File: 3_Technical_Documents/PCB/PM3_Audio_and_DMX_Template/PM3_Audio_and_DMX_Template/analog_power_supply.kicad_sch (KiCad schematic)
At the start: 16 parts, among them U6 TLV61070ADBV, U7 LT3045xMSE

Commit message: new push
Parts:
- renumbered C18 to C19, C19 to C20, C20 to C21, C21 to C22, C22 to C23, C23 to C24, C24 to C25, R25 to R21, R26 to R22, R27 to R23, R28 to R24, R29 to R25, R30 to R26, U6 to U7, U7 to U8
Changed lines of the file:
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@@
 		(dnp no)
 		(fields_autoplaced yes)
-		(property "Reference" "#PWR050"
+		(property "Reference" "#PWR058"
 			(at 92.71 106.68 0)
 			(effects
@@
 			(project ""
 				(path "/1f276d59-ad9b-4e70-a842-f3b7e562eb9b/2329d9ea-d5d7-4913-84c5-e85a54af032e/99ea690b-15c6-4a9d-8469-e6d453aade26"
-					(reference "#PWR050")
+					(reference "#PWR058")
 					(unit 1)
 				)
@@
 		(dnp no)
 		(fields_autoplaced yes)
-		(property "Reference" "R25"
+		(property "Reference" "R21"
 			(at 95.25 81.2799 0)
 			(effects
@@
 			(project ""
 				(path "/1f276d59-ad9b-4e70-a842-f3b7e562eb9b/2329d9ea-d5d7-4913-84c5-e85a54af032e/99ea690b-15c6-4a9d-8469-e6d453aade26"
-					(reference "R25")
+					(reference "R21")
 					(unit 1)
 				)
@@
 		(dnp no)
 		(fields_autoplaced yes)
-		(property "Reference" "U6"
+		(property "Reference" "U7"
 			(at 74.93 66.04 0)
 			(effects
@@
 			(project ""
 				(path "/1f276d59-ad9b-4e70-a842-f3b7e562eb9b/2329d9ea-d5d7-4913-84c5-e85a54af032e/99ea690b-15c6-4a9d-8469-e6d453aade26"
-					(reference "U6")
+					(reference "U7")
 					(unit 1)
 				)
@@
 		(dnp no)
 		(fields_autoplaced yes)
-		(property "Reference" "C18"
+		(property "Reference" "C19"
 			(at 40.64 77.8509 0)
 			(effects
@@
 			(project ""
 				(path "/1f276d59-ad9b-4e70-a842-f3b7e562eb9b/2329d9ea-d5d7-4913-84c5-e85a54af032e/99ea690b-15c6-4a9d-8469-e6d453aade26"
-					(reference "C18")
+					(reference "C19")
 					(unit 1)
 				)
@@
 		(dnp no)
 		(fields_autoplaced yes)
-		(property "Reference" "#PWR049"
+		(property "Reference" "#PWR057"
 			(at 74.93 97.79 0)
 			(effects
@@
 			(project ""
 				(path "/1f276d59-ad9b-4e70-a842-f3b7e562eb9b/2329d9ea-d5d7-4913-84c5-e85a54af032e/99ea690b-15c6-4a9d-8469-e6d453aade26"
-					(reference "#PWR049")
+					(reference "#PWR057")
 					(unit 1)
 				)
@@
 		(dnp no)
 		(fields_autoplaced yes)
-		(property "Reference" "#PWR057"
+		(property "Reference" "#PWR065"
 			(at 212.09 90.17 0)
 			(effects
@@
 			(project ""
 				(path "/1f276d59-ad9b-4e70-a842-f3b7e562eb9b/2329d9ea-d5d7-4913-84c5-e85a54af032e/99ea690b-15c6-4a9d-8469-e6d453aade26"
-					(reference "#PWR057")
+					(reference "#PWR065")
 					(unit 1)
 				)
@@
 		(on_board yes)
 		(dnp no)
-		(property "Reference" "C23"
+		(property "Reference" "C24"
 			(at 167.132 60.706 90)
 			(effects
@@
 			(project "PM3_Audio_and_DMX"
 				(path "/1f276d59-ad9b-4e70-a842-f3b7e562eb9b/2329d9ea-d5d7-4913-84c5-e85a54af032e/99ea690b-15c6-4a9d-8469-e6d453aade26"
-					(reference "C23")
+					(reference "C24")
 					(unit 1)
 				)
@@
 		(dnp no)
 		(fields_autoplaced yes)
-		(property "Reference" "R28"
+		(property "Reference" "R24"
 			(at 200.66 58.4199 0)
 			(effects
@@
 			(project ""
 				(path "/1f276d59-ad9b-4e70-a842-f3b7e562eb9b/2329d9ea-d5d7-4913-84c5-e85a54af032e/99ea690b-15c6-4a9d-8469-e6d453aade26"
-					(reference "R28")
+					(reference "R24")
 					(unit 1)
 				)
@@
 		(dnp no)
 		(fields_autoplaced yes)
-		(property "Reference" "#PWR052"
+		(property "Reference" "#PWR060"
 			(at 156.21 74.93 0)
 			(effects
@@
 			(project "PM3_Audio_and_DMX"
 				(path "/1f276d59-ad9b-4e70-a842-f3b7e562eb9b/2329d9ea-d5d7-4913-84c5-e85a54af032e/99ea690b-15c6-4a9d-8469-e6d453aade26"
-					(reference "#PWR052")
+					(reference "#PWR060")
 					(unit 1)
 				)
@@
 		(dnp no)
 		(fields_autoplaced yes)
-		(property "Reference" "R30"
+		(property "Reference" "R26"
 			(at 205.74 87.6299 0)
 			(effects
@@
 			(project ""
 				(path "/1f276d59-ad9b-4e70-a842-f3b7e562eb9b/2329d9ea-d5d7-4913-84c5-e85a54af032e/99ea690b-15c6-4a9d-8469-e6d453aade26"
-					(reference "R30")
+					(reference "R26")
 					(unit 1)
 				)
@@
 		(dnp no)
 		(fields_autoplaced yes)
-		(property "Reference" "#PWR051"
+		(property "Reference" "#PWR059"
 			(at 118.11 97.79 0)
 			(effects
@@
 			(project ""
 				(path "/1f276d59-ad9b-4e70-a842-f3b7e562eb9b/2329d9ea-d5d7-4913-84c5-e85a54af032e/99ea690b-15c6-4a9d-8469-e6d453aade26"
-					(reference "#PWR051")
+					(reference "#PWR059")
 					(unit 1)
 				)
@@
 		(dnp no)
 		(fields_autoplaced yes)
-		(property "Reference" "#PWR055"
+		(property "Reference" "#PWR063"
 			(at 185.42 91.44 0)
 			(effects
@@
 			(project ""
 				(path "/1f276d59-ad9b-4e70-a842-f3b7e562eb9b/2329d9ea-d5d7-4913-84c5-e85a54af032e/99ea690b-15c6-4a9d-8469-e6d453aade26"
-					(reference "#PWR055")
+					(reference "#PWR063")
 					(unit 1)
 				)
@@
 		(dnp no)
 		(fields_autoplaced yes)
-		(property "Reference" "#PWR054"
+		(property "Reference" "#PWR062"
 			(at 162.56 73.66 0)
 			(effects
@@
 			(project ""
 				(path "/1f276d59-ad9b-4e70-a842-f3b7e562eb9b/2329d9ea-d5d7-4913-84c5-e85a54af032e/99ea690b-15c6-4a9d-8469-e6d453aade26"
-					(reference "#PWR054")
+					(reference "#PWR062")
 					(unit 1)
 				)
@@
 		(dnp no)
 		(fields_autoplaced yes)
-		(property "Reference" "R29"
+		(property "Reference" "R25"
 			(at 205.74 77.4699 0)
 			(effects
@@
 			(project ""
 				(path "/1f276d59-ad9b-4e70-a842-f3b7e562eb9b/2329d9ea-d5d7-4913-84c5-e85a54af032e/99ea690b-15c6-4a9d-8469-e6d453aade26"
-					(reference "R29")
+					(reference "R25")
 					(unit 1)
 				)
@@
 		(dnp no)
 		(fields_autoplaced yes)
-		(property "Reference" "#PWR048"
+		(property "Reference" "#PWR056"
 			(at 52.07 93.98 0)
 			(effects
@@
 			(project ""
 				(path "/1f276d59-ad9b-4e70-a842-f3b7e562eb9b/2329d9ea-d5d7-4913-84c5-e85a54af032e/99ea690b-15c6-4a9d-8469-e6d453aade26"
-					(reference "#PWR048")
+					(reference "#PWR056")
 					(unit 1)
 				)
@@
 		(dnp no)
 		(fields_autoplaced yes)
-		(property "Reference" "#PWR047"
+		(property "Reference" "#PWR055"
 			(at 36.83 95.25 0)
 			(effects
@@
 			(project ""
 				(path "/1f276d59-ad9b-4e70-a842-f3b7e562eb9b/2329d9ea-d5d7-4913-84c5-e85a54af032e/99ea690b-15c6-4a9d-8469-e6d453aade26"
-					(reference "#PWR047")
+					(reference "#PWR055")
 					(unit 1)
 				)
@@
 		(dnp no)
 		(fields_autoplaced yes)
-		(property "Reference" "C22"
+		(property "Reference" "C23"
 			(at 153.67 81.2799 0)
 			(effects
@@
 			(project ""
 				(path "/1f276d59-ad9b-4e70-a842-f3b7e562eb9b/2329d9ea-d5d7-4913-84c5-e85a54af032e/99ea690b-15c6-4a9d-8469-e6d453aade26"
-					(reference "C22")
+					(reference "C23")
 					(unit 1)
 				)
@@
 		(dnp no)
 		(fields_autoplaced yes)
-		(property "Reference" "C19"
+		(property "Reference" "C20"
 			(at 55.88 78.7399 0)
 			(effects
@@
 			(project ""
 				(path "/1f276d59-ad9b-4e70-a842-f3b7e562eb9b/2329d9ea-d5d7-4913-84c5-e85a54af032e/99ea690b-15c6-4a9d-8469-e6d453aade26"
-					(reference "C19")
+					(reference "C20")
 					(unit 1)
 				)
@@
 		(dnp no)
 		(fields_autoplaced yes)
-		(property "Reference" "#PWR056"
+		(property "Reference" "#PWR064"
 			(at 203.2 102.87 0)
 			(effects
@@
 			(project ""
 				(path "/1f276d59-ad9b-4e70-a842-f3b7e562eb9b/2329d9ea-d5d7-4913-84c5-e85a54af032e/99ea690b-15c6-4a9d-8469-e6d453aade26"
-					(reference "#PWR056")
+					(reference "#PWR064")
 					(unit 1)
 				)
@@
 		(dnp no)
 		(fields_autoplaced yes)
-		(property "Reference" "R26"
+		(property "Reference" "R22"
 			(at 95.25 91.4399 0)
 			(effects
@@
 			(project ""
 				(path "/1f276d59-ad9b-4e70-a842-f3b7e562eb9b/2329d9ea-d5d7-4913-84c5-e85a54af032e/99ea690b-15c6-4a9d-8469-e6d453aade26"
-					(reference "R26")
+					(reference "R22")
 					(unit 1)
 				)
@@
 		(dnp no)
 		(fields_autoplaced yes)
-		(property "Reference" "C24"
+		(property "Reference" "C25"
 			(at 215.9 73.6599 0)
 			(effects
@@
 			(project ""
 				(path "/1f276d59-ad9b-4e70-a842-f3b7e562eb9b/2329d9ea-d5d7-4913-84c5-e85a54af032e/99ea690b-15c6-4a9d-8469-e6d453aade26"
-					(reference "C24")
+					(reference "C25")
 					(unit 1)
 				)
@@
 		(dnp no)
 		(fields_autoplaced yes)
-		(property "Reference" "#PWR053"
+		(property "Reference" "#PWR061"
 			(at 165.1 101.6 0)
 			(effects
@@
 			(project "PM3_Audio_and_DMX"
 				(path "/1f276d59-ad9b-4e70-a842-f3b7e562eb9b/2329d9ea-d5d7-4913-84c5-e85a54af032e/99ea690b-15c6-4a9d-8469-e6d453aade26"
-					(reference "#PWR053")
+					(reference "#PWR061")
 					(unit 1)
 				)
@@
 		(dnp no)
 		(fields_autoplaced yes)
-		(property "Reference" "U7"
+		(property "Reference" "U8"
 			(at 185.42 60.96 0)
 			(effects
@@
 			(project ""
 				(path "/1f276d59-ad9b-4e70-a842-f3b7e562eb9b/2329d9ea-d5d7-4913-84c5-e85a54af032e/99ea690b-15c6-4a9d-8469-e6d453aade26"
-					(reference "U7")
+					(reference "U8")
 					(unit 1)
 				)
@@
 		(dnp no)
 		(fields_autoplaced yes)
-		(property "Reference" "C20"
+		(property "Reference" "C21"
 			(at 107.95 81.2799 0)
 			(effects
@@
 			(project ""
 				(path "/1f276d59-ad9b-4e70-a842-f3b7e562eb9b/2329d9ea-d5d7-4913-84c5-e85a54af032e/99ea690b-15c6-4a9d-8469-e6d453aade26"
-					(reference "C20")
+					(reference "C21")
 					(unit 1)
 				)
@@
 		(dnp no)
 		(fields_autoplaced yes)
-		(property "Reference" "C21"
+		(property "Reference" "C22"
 			(at 121.92 82.5499 0)
 			(effects
@@
 			(project ""
 				(path "/1f276d59-ad9b-4e70-a842-f3b7e562eb9b/2329d9ea-d5d7-4913-84c5-e85a54af032e/99ea690b-15c6-4a9d-8469-e6d453aade26"
-					(reference "C21")
+					(reference "C22")
 					(unit 1)
 				)
@@
 		(dnp no)
 		(fields_autoplaced yes)
-		(property "Reference" "R27"
+		(property "Reference" "R23"
 			(at 167.64 81.2799 0)
 			(effects
@@
 			(project ""
 				(path "/1f276d59-ad9b-4e70-a842-f3b7e562eb9b/2329d9ea-d5d7-4913-84c5-e85a54af032e/99ea690b-15c6-4a9d-8469-e6d453aade26"
-					(reference "R27")
-					(unit 1)
-				)
+					(reference "R23")
+					(unit 1)
+				)

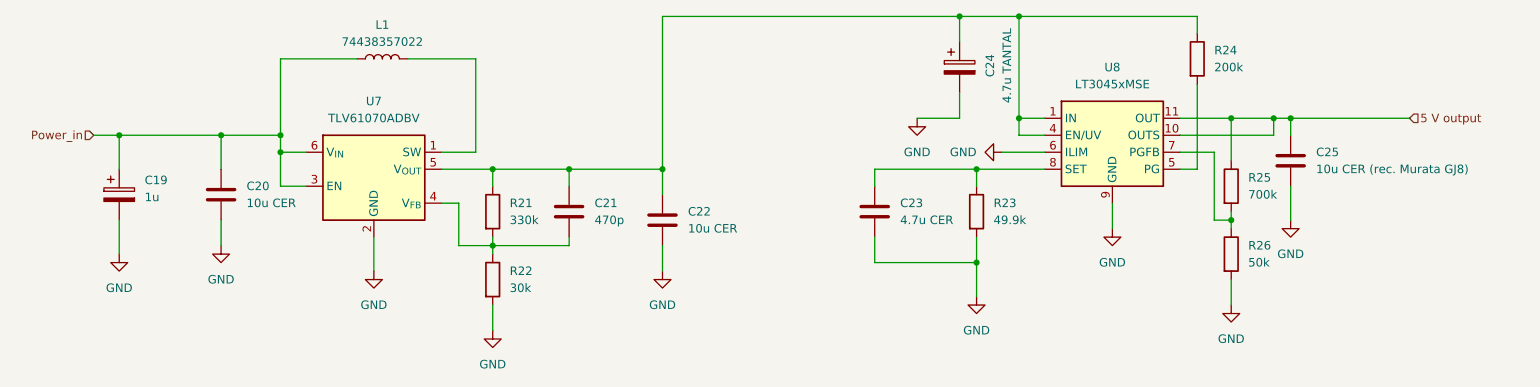
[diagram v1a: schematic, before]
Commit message: rework esp32, codec and layout
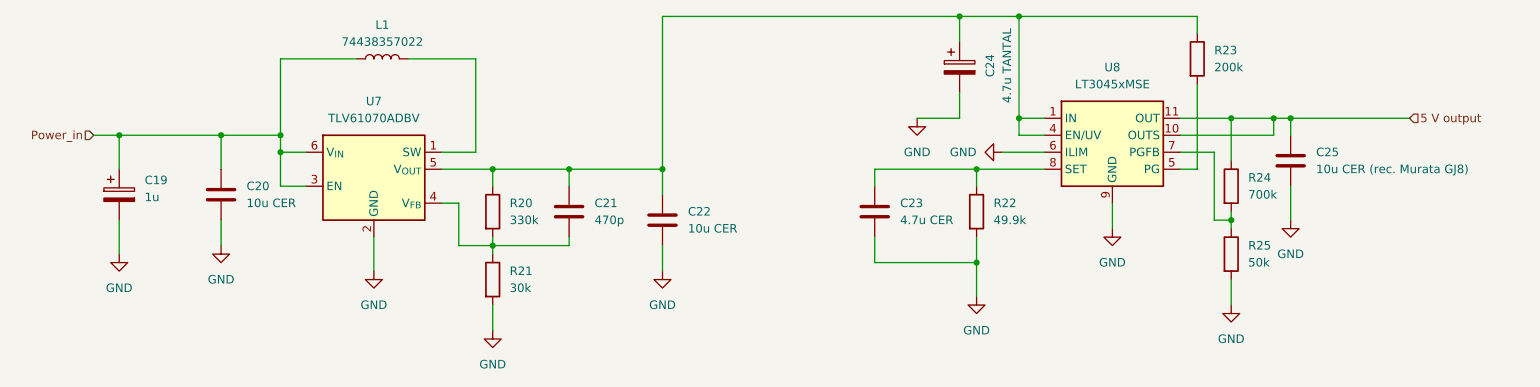
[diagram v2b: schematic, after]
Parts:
- renumbered R21 to R20, R22 to R21, R23 to R22, R24 to R23, R25 to R24, R26 to R25
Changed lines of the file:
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@@
 		(dnp no)
 		(fields_autoplaced yes)
-		(property "Reference" "#PWR058"
+		(property "Reference" "#PWR057"
 			(at 92.71 106.68 0)
 			(effects
@@
 			(project ""
 				(path "/1f276d59-ad9b-4e70-a842-f3b7e562eb9b/2329d9ea-d5d7-4913-84c5-e85a54af032e/99ea690b-15c6-4a9d-8469-e6d453aade26"
-					(reference "#PWR058")
+					(reference "#PWR057")
 					(unit 1)
 				)
@@
 		(dnp no)
 		(fields_autoplaced yes)
-		(property "Reference" "R21"
+		(property "Reference" "R20"
 			(at 95.25 81.2799 0)
 			(effects
@@
 			(project ""
 				(path "/1f276d59-ad9b-4e70-a842-f3b7e562eb9b/2329d9ea-d5d7-4913-84c5-e85a54af032e/99ea690b-15c6-4a9d-8469-e6d453aade26"
-					(reference "R21")
+					(reference "R20")
 					(unit 1)
 				)
@@
 		(dnp no)
 		(fields_autoplaced yes)
-		(property "Reference" "#PWR057"
+		(property "Reference" "#PWR056"
 			(at 74.93 97.79 0)
 			(effects
@@
 			(project ""
 				(path "/1f276d59-ad9b-4e70-a842-f3b7e562eb9b/2329d9ea-d5d7-4913-84c5-e85a54af032e/99ea690b-15c6-4a9d-8469-e6d453aade26"
-					(reference "#PWR057")
+					(reference "#PWR056")
 					(unit 1)
 				)
@@
 		(dnp no)
 		(fields_autoplaced yes)
-		(property "Reference" "#PWR065"
+		(property "Reference" "#PWR064"
 			(at 212.09 90.17 0)
 			(effects
@@
 			(project ""
 				(path "/1f276d59-ad9b-4e70-a842-f3b7e562eb9b/2329d9ea-d5d7-4913-84c5-e85a54af032e/99ea690b-15c6-4a9d-8469-e6d453aade26"
-					(reference "#PWR065")
+					(reference "#PWR064")
 					(unit 1)
 				)
@@
 		(dnp no)
 		(fields_autoplaced yes)
-		(property "Reference" "R24"
+		(property "Reference" "R23"
 			(at 200.66 58.4199 0)
 			(effects
@@
 			(project ""
 				(path "/1f276d59-ad9b-4e70-a842-f3b7e562eb9b/2329d9ea-d5d7-4913-84c5-e85a54af032e/99ea690b-15c6-4a9d-8469-e6d453aade26"
-					(reference "R24")
+					(reference "R23")
 					(unit 1)
 				)
@@
 		(dnp no)
 		(fields_autoplaced yes)
-		(property "Reference" "#PWR060"
+		(property "Reference" "#PWR059"
 			(at 156.21 74.93 0)
 			(effects
@@
 			(project "PM3_Audio_and_DMX"
 				(path "/1f276d59-ad9b-4e70-a842-f3b7e562eb9b/2329d9ea-d5d7-4913-84c5-e85a54af032e/99ea690b-15c6-4a9d-8469-e6d453aade26"
-					(reference "#PWR060")
+					(reference "#PWR059")
 					(unit 1)
 				)
@@
 		(dnp no)
 		(fields_autoplaced yes)
-		(property "Reference" "R26"
+		(property "Reference" "R25"
 			(at 205.74 87.6299 0)
 			(effects
@@
 			(project ""
 				(path "/1f276d59-ad9b-4e70-a842-f3b7e562eb9b/2329d9ea-d5d7-4913-84c5-e85a54af032e/99ea690b-15c6-4a9d-8469-e6d453aade26"
-					(reference "R26")
+					(reference "R25")
 					(unit 1)
 				)
@@
 		(dnp no)
 		(fields_autoplaced yes)
-		(property "Reference" "#PWR059"
+		(property "Reference" "#PWR058"
 			(at 118.11 97.79 0)
 			(effects
@@
 			(project ""
 				(path "/1f276d59-ad9b-4e70-a842-f3b7e562eb9b/2329d9ea-d5d7-4913-84c5-e85a54af032e/99ea690b-15c6-4a9d-8469-e6d453aade26"
-					(reference "#PWR059")
+					(reference "#PWR058")
 					(unit 1)
 				)
@@
 		(dnp no)
 		(fields_autoplaced yes)
-		(property "Reference" "#PWR063"
+		(property "Reference" "#PWR062"
 			(at 185.42 91.44 0)
 			(effects
@@
 			(project ""
 				(path "/1f276d59-ad9b-4e70-a842-f3b7e562eb9b/2329d9ea-d5d7-4913-84c5-e85a54af032e/99ea690b-15c6-4a9d-8469-e6d453aade26"
-					(reference "#PWR063")
+					(reference "#PWR062")
 					(unit 1)
 				)
@@
 		(dnp no)
 		(fields_autoplaced yes)
-		(property "Reference" "#PWR062"
+		(property "Reference" "#PWR061"
 			(at 162.56 73.66 0)
 			(effects
@@
 			(project ""
 				(path "/1f276d59-ad9b-4e70-a842-f3b7e562eb9b/2329d9ea-d5d7-4913-84c5-e85a54af032e/99ea690b-15c6-4a9d-8469-e6d453aade26"
-					(reference "#PWR062")
+					(reference "#PWR061")
 					(unit 1)
 				)
@@
 		(dnp no)
 		(fields_autoplaced yes)
-		(property "Reference" "R25"
+		(property "Reference" "R24"
 			(at 205.74 77.4699 0)
 			(effects
@@
 			(project ""
 				(path "/1f276d59-ad9b-4e70-a842-f3b7e562eb9b/2329d9ea-d5d7-4913-84c5-e85a54af032e/99ea690b-15c6-4a9d-8469-e6d453aade26"
-					(reference "R25")
+					(reference "R24")
 					(unit 1)
 				)
@@
 		(dnp no)
 		(fields_autoplaced yes)
-		(property "Reference" "#PWR056"
+		(property "Reference" "#PWR055"
 			(at 52.07 93.98 0)
 			(effects
@@
 			(project ""
 				(path "/1f276d59-ad9b-4e70-a842-f3b7e562eb9b/2329d9ea-d5d7-4913-84c5-e85a54af032e/99ea690b-15c6-4a9d-8469-e6d453aade26"
-					(reference "#PWR056")
+					(reference "#PWR055")
 					(unit 1)
 				)
@@
 		(dnp no)
 		(fields_autoplaced yes)
-		(property "Reference" "#PWR055"
+		(property "Reference" "#PWR054"
 			(at 36.83 95.25 0)
 			(effects
@@
 			(project ""
 				(path "/1f276d59-ad9b-4e70-a842-f3b7e562eb9b/2329d9ea-d5d7-4913-84c5-e85a54af032e/99ea690b-15c6-4a9d-8469-e6d453aade26"
-					(reference "#PWR055")
+					(reference "#PWR054")
 					(unit 1)
 				)
@@
 		(dnp no)
 		(fields_autoplaced yes)
-		(property "Reference" "#PWR064"
+		(property "Reference" "#PWR063"
 			(at 203.2 102.87 0)
 			(effects
@@
 			(project ""
 				(path "/1f276d59-ad9b-4e70-a842-f3b7e562eb9b/2329d9ea-d5d7-4913-84c5-e85a54af032e/99ea690b-15c6-4a9d-8469-e6d453aade26"
-					(reference "#PWR064")
+					(reference "#PWR063")
 					(unit 1)
 				)
@@
 		(dnp no)
 		(fields_autoplaced yes)
-		(property "Reference" "R22"
+		(property "Reference" "R21"
 			(at 95.25 91.4399 0)
 			(effects
@@
 			(project ""
 				(path "/1f276d59-ad9b-4e70-a842-f3b7e562eb9b/2329d9ea-d5d7-4913-84c5-e85a54af032e/99ea690b-15c6-4a9d-8469-e6d453aade26"
-					(reference "R22")
+					(reference "R21")
 					(unit 1)
 				)
@@
 		(dnp no)
 		(fields_autoplaced yes)
-		(property "Reference" "#PWR061"
+		(property "Reference" "#PWR060"
 			(at 165.1 101.6 0)
 			(effects
@@
 			(project "PM3_Audio_and_DMX"
 				(path "/1f276d59-ad9b-4e70-a842-f3b7e562eb9b/2329d9ea-d5d7-4913-84c5-e85a54af032e/99ea690b-15c6-4a9d-8469-e6d453aade26"
-					(reference "#PWR061")
+					(reference "#PWR060")
 					(unit 1)
 				)
@@
 		(dnp no)
 		(fields_autoplaced yes)
-		(property "Reference" "R23"
+		(property "Reference" "R22"
 			(at 167.64 81.2799 0)
 			(effects
@@
 			(project ""
 				(path "/1f276d59-ad9b-4e70-a842-f3b7e562eb9b/2329d9ea-d5d7-4913-84c5-e85a54af032e/99ea690b-15c6-4a9d-8469-e6d453aade26"
-					(reference "R23")
-					(unit 1)
-				)
+					(reference "R22")
+					(unit 1)
+				)

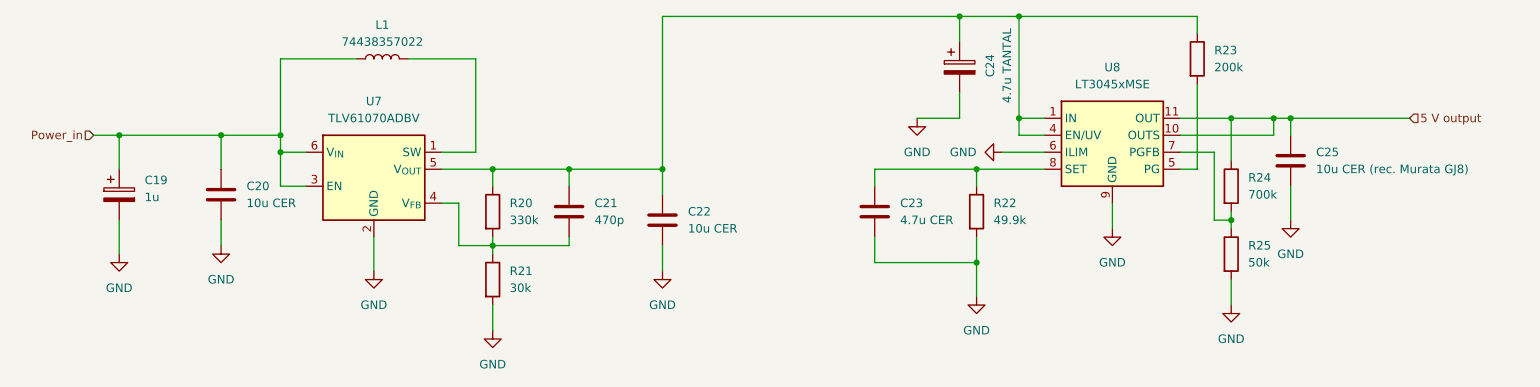
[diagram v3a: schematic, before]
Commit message: schematics, layout and bom updated (to match corrections)
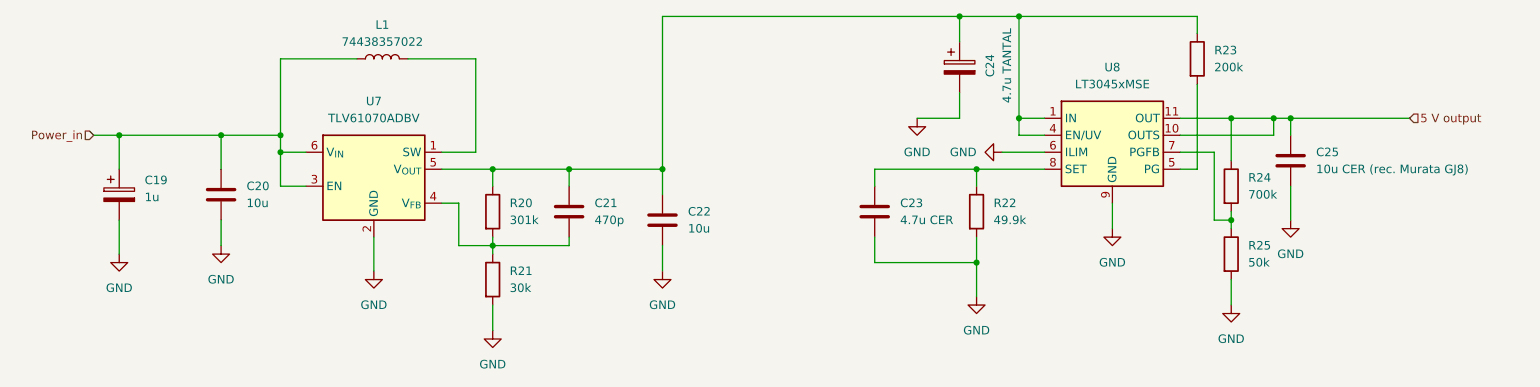
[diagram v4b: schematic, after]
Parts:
- C20, C22: value 10u CER -> 10u
- R20: value 330k -> 301k; MPN GPR0603330K -> (none)
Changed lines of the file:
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@@
 			)
 		)
-		(property "Value" "330k"
+		(property "Value" "301k"
 			(at 95.25 83.8199 0)
 			(effects
@@
 			)
 		)
-		(property "Datasheet" "~"
+		(property "Datasheet" ""
 			(at 92.71 82.55 0)
 			(effects
@@
 			)
 		)
-		(property "MPN" "GPR0603330K"
+		(property "MPN" ""
 			(at 92.71 82.55 0)
 			(effects
@@
 			)
 		)
-		(property "Value" "10u CER"
+		(property "Value" "10u"
 			(at 55.88 81.2799 0)
 			(effects
@@
 			)
 		)
-		(property "Value" "10u CER"
+		(property "Value" "10u"
 			(at 121.92 85.0899 0)
 			(effects
